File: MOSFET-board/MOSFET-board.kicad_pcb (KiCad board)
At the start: 2 copper layers, 88.9 x 76.2 mm, 116 parts, among them J1 PCIE-LP-01-01-F-DV-A-TR, J2 DB15_Female, J3 DB15_Female, U1 BTS3080EJXUMA1, U10 BTS3080EJXUMA1, U11 PCF8575_Breakout, U12 INA193, U13 INA193, U14 INA193, U15 INA193, U16 INA193, U17 INA193, U18 INA193, U19 INA193, U2 BTS3080EJXUMA1, U20 INA193, U21 INA193, U3 BTS3080EJXUMA1, U4 BTS3080EJXUMA1, U5 BTS3080EJXUMA1, U6 BTS3080EJXUMA1, U7 BTS3080EJXUMA1, U8 BTS3080EJXUMA1, U9 BTS3080EJXUMA1

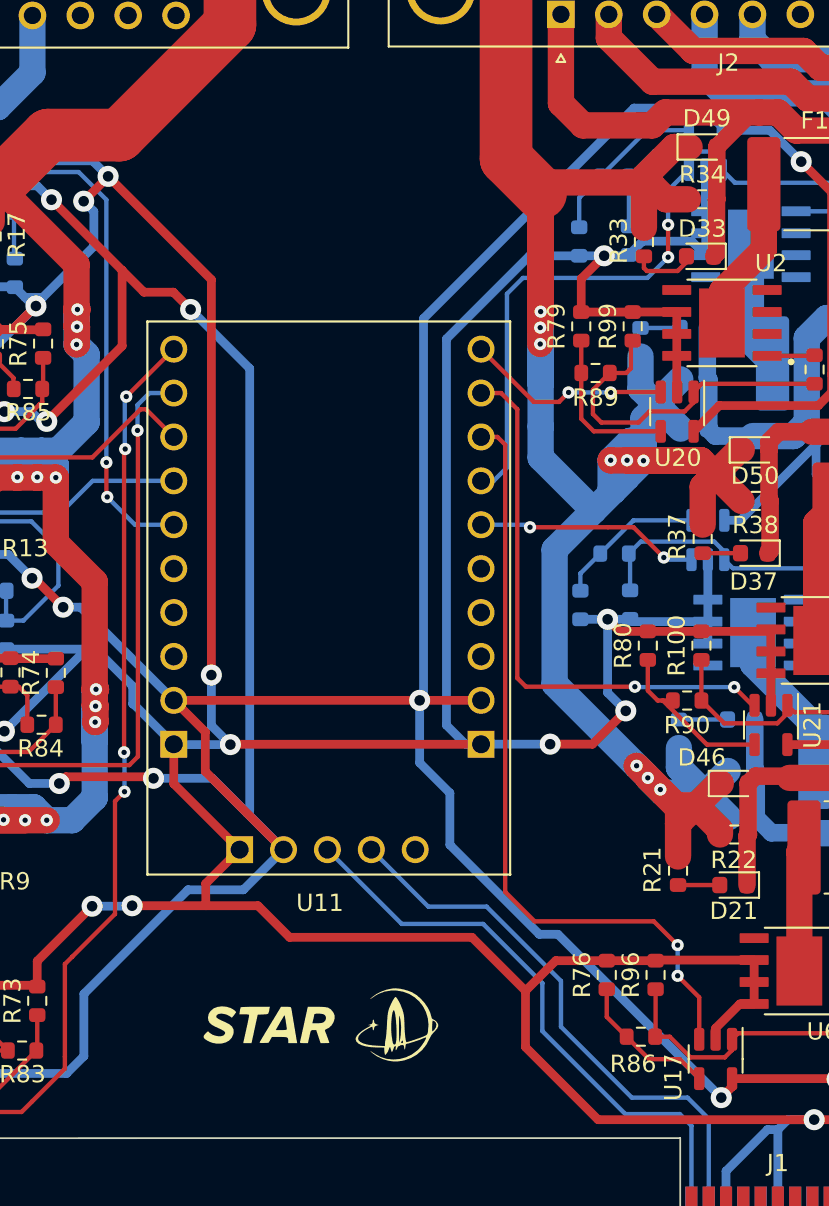
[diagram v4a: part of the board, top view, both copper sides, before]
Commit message: MOSFET Board Updated (Part II)
Added double header GPIO and should be fine now :P
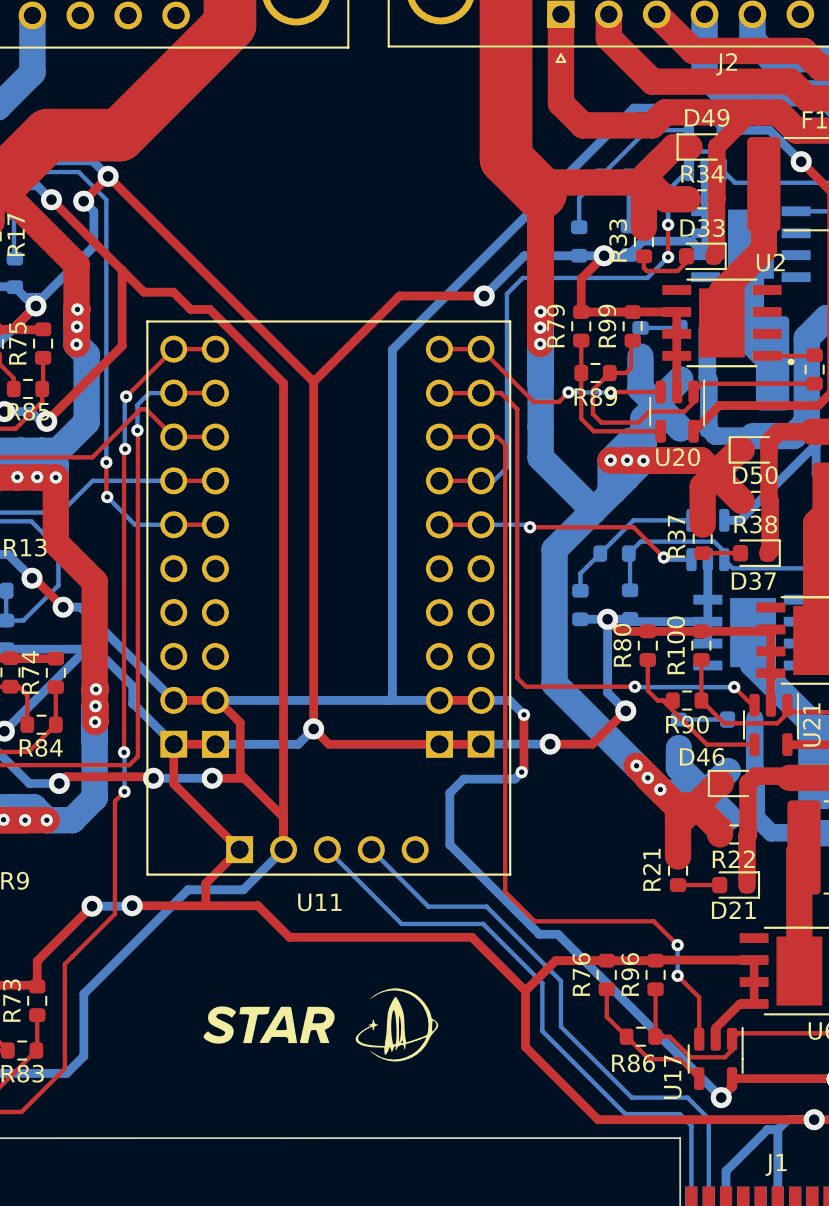
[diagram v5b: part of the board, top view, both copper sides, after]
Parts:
- added ?: , , F.Cu at (169.0, 104.2)
- added ?: , , F.Cu at (156.0, 94.0)
- added ?: , , F.Cu at (169.0, 116.9)
- added ?: , , F.Cu at (156.0, 114.4)
- added ?: , , F.Cu at (156.0, 104.2)
- added ?: , , F.Cu at (169.0, 101.7)
- added ?: , , F.Cu at (169.0, 99.1)
- added ?: , , F.Cu at (169.0, 111.8)
- added ?: , , F.Cu at (156.0, 106.8)
- added ?: , , F.Cu at (156.0, 101.7)
- added ?: , , F.Cu at (169.0, 114.4)
- added ?: , , F.Cu at (156.0, 116.9)
- added ?: , , F.Cu at (156.0, 96.6)
- added ?: , , F.Cu at (156.0, 111.8)
- added ?: , , F.Cu at (156.0, 99.1)
- added ?: , , F.Cu at (169.0, 94.0)
- added ?: , , F.Cu at (156.0, 109.3)
- added ?: , , F.Cu at (169.0, 106.8)
- added ?: , , F.Cu at (169.0, 109.3)
- added ?: , , F.Cu at (169.0, 96.6)
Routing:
- net GND: track 449.1 -> 434.8 mm
- net +5V: track 332.0 -> 336.7 mm, vias 16 -> 17
- net PYRO3EN: track 36.4 -> 38.8 mm
- net PYRO9EN: track 35.1 -> 37.6 mm
- net PYRO1EN: track 53.7 -> 56.1 mm
- net PYRO6EN: track 44.7 -> 47.1 mm
- net PYRO10EN: track 13.0 -> 15.4 mm
- net PYRO7EN: track 18.8 -> 21.2 mm
- net PYRO5EN: track 17.4 -> 19.8 mm
- net PYRO8EN: track 27.6 -> 30.0 mm
- net PYRO4EN: track 32.4 -> 34.8 mm
- net PYRO2EN: track 11.9 -> 14.3 mm

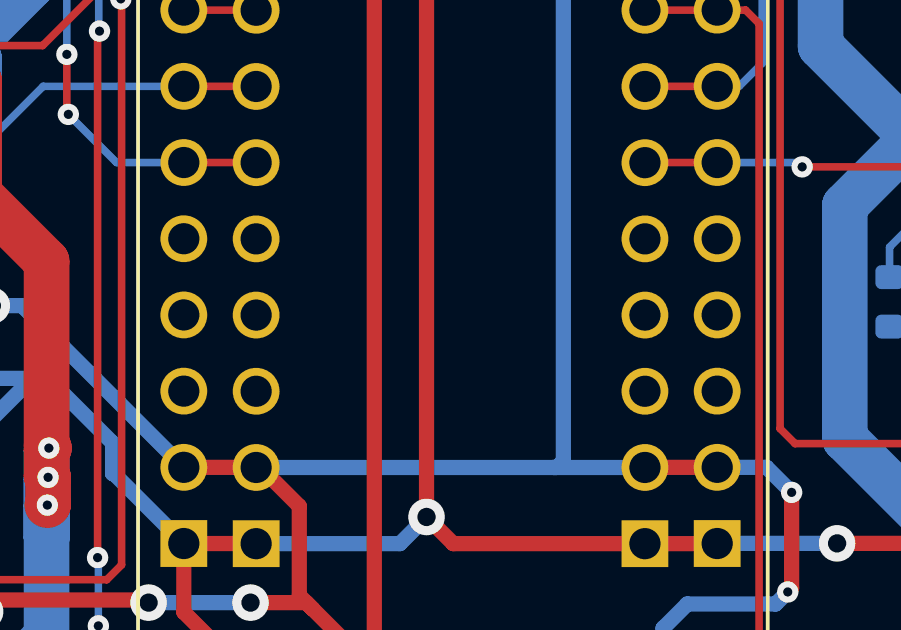
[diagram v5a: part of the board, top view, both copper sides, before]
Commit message: Updated MOSFET (part III)
Made sure there were 0 errors.
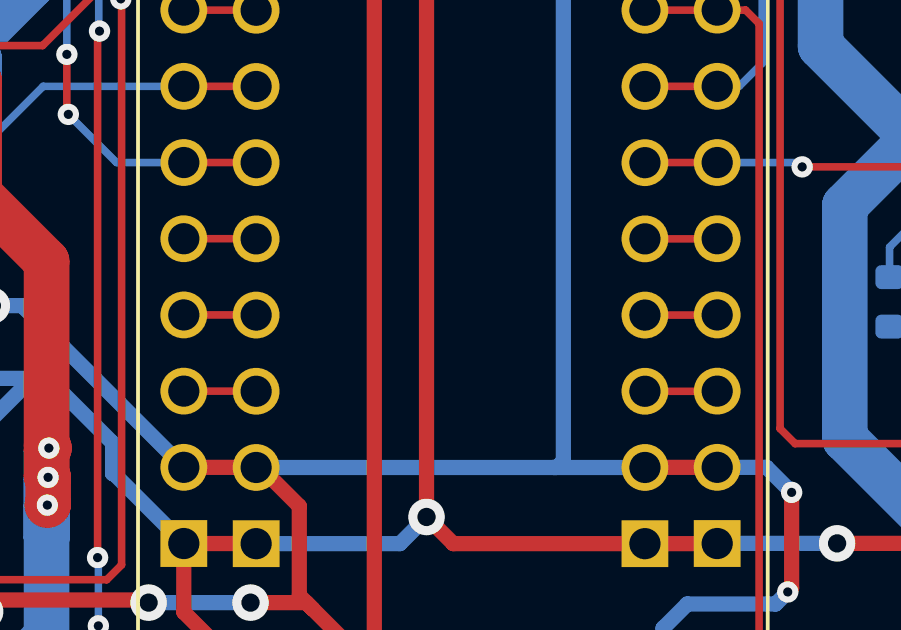
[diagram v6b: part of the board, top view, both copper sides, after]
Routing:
- net unconnected-(U11-P16-Pad7): track 0.00 -> 2.41 mm
- net unconnected-(U11-P17-Pad8): track 0.00 -> 2.41 mm
- net unconnected-(U11-P15-Pad6): track 0.00 -> 2.41 mm
- net unconnected-(U11-P01-Pad19): track 0.00 -> 2.41 mm
- net unconnected-(U11-P02-Pad20): track 0.00 -> 2.41 mm
- net unconnected-(U11-P00-Pad18): track 0.00 -> 2.41 mm
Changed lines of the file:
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@@
   (segment (start 195.45 112.9) (end 195.45 112.875) (width 0.254) (layer "F.Cu") (net 104))
   (segment (start 195.95 113.4) (end 195.45 112.9) (width 0.254) (layer "F.Cu") (net 104))
+  (segment (start 153.5989 106.7455) (end 156.0055 106.7455) (width 0.254) (layer "F.Cu") (net 145))
+  (segment (start 156.0055 106.7455) (end 156.01 106.75) (width 0.254) (layer "F.Cu") (net 145))
+  (segment (start 156.0055 109.2855) (end 156.01 109.29) (width 0.254) (layer "F.Cu") (net 146))
+  (segment (start 153.5989 109.2855) (end 156.0055 109.2855) (width 0.254) (layer "F.Cu") (net 146))
+  (segment (start 156.0055 111.8255) (end 156.01 111.83) (width 0.254) (layer "F.Cu") (net 147))
+  (segment (start 153.5989 111.8255) (end 156.0055 111.8255) (width 0.254) (layer "F.Cu") (net 147))
+  (segment (start 168.97 111.83) (end 171.37384 111.83) (width 0.254) (layer "F.Cu") (net 149))
+  (segment (start 171.37384 111.83) (end 171.37834 111.8255) (width 0.254) (layer "F.Cu") (net 149))
+  (segment (start 171.37384 109.29) (end 171.37834 109.2855) (width 0.254) (layer "F.Cu") (net 150))
+  (segment (start 168.97 109.29) (end 171.37384 109.29) (width 0.254) (layer "F.Cu") (net 150))
+  (segment (start 171.37384 106.75) (end 171.37834 106.7455) (width 0.254) (layer "F.Cu") (net 151))
+  (segment (start 168.97 106.75) (end 171.37384 106.75) (width 0.254) (layer "F.Cu") (net 151))
   (zone (net 25) (net_name "GND") (layers "F&B.Cu") (hatch edge 0.508)
     (connect_pads (clearance 0.508))

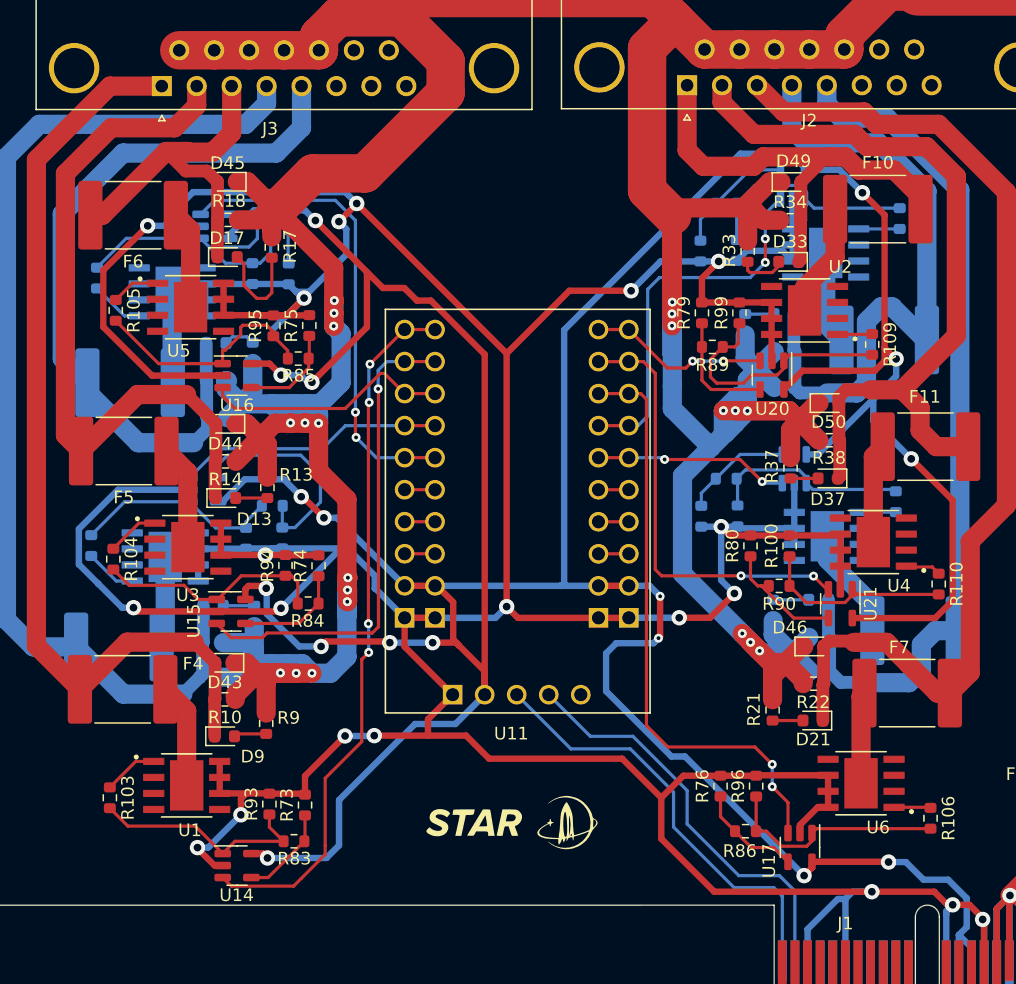
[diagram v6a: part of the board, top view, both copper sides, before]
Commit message: MOSFET Board Updated (Part IV? I lost count)
Has a specified op amp, fixed measurements, should be a double header GPIO, I believe that everything is connected. The only warnings are either silk screen or non labeled items, which should be fine.
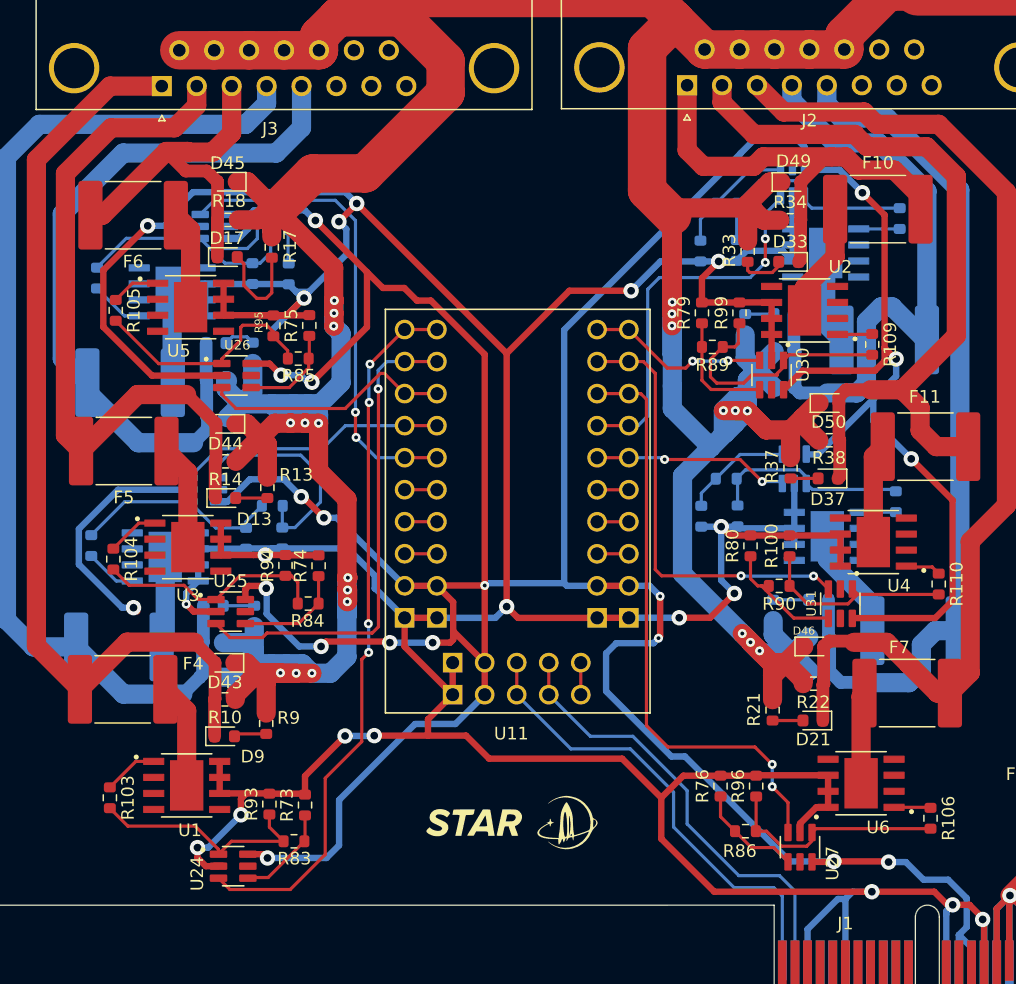
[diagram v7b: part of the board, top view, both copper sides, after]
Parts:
- removed U12, U13, U14, U15, U16, U17, U18, U19, U20, U21: INA193, Package_TO_SOT_SMD:SOT-23-5
- added ?: , , F.Cu at (159.9, 120.5)
- added ?: , , F.Cu at (157.4, 120.5)
- added ?: , , F.Cu at (162.5, 120.5)
- added ?: , , F.Cu at (165.0, 120.5)
- added ?: , , F.Cu at (167.6, 120.5)
- added U22: ADA4897-1ARJZ-R7, Symbol:SOT95P280X145-6N, B.Cu at (137.7, 106.8)
- added U23: ADA4897-1ARJZ-R7, Symbol:SOT95P280X145-6N, B.Cu at (138.6, 85.9)
- added U24: ADA4897-1ARJZ-R7, Symbol:SOT95P280X145-6N, F.Cu at (140.0, 136.6)
- added U25: ADA4897-1ARJZ-R7, Symbol:SOT95P280X145-6N, F.Cu at (139.8, 116.4)
- added U26: ADA4897-1ARJZ-R7, Symbol:SOT95P280X145-6N, F.Cu at (140.3, 97.7)
- added U27: ADA4897-1ARJZ-R7, Symbol:SOT95P280X145-6N, F.Cu at (184.9, 135.1)
- added U28: ADA4897-1ARJZ-R7, Symbol:SOT95P280X145-6N, B.Cu at (184.4, 82.3)
- added U29: ADA4897-1ARJZ-R7, Symbol:SOT95P280X145-6N, B.Cu at (184.5, 105.1)
- added U30: ADA4897-1ARJZ-R7, Symbol:SOT95P280X145-6N, F.Cu at (182.7, 97.7)
- added U31: ADA4897-1ARJZ-R7, Symbol:SOT95P280X145-6N, F.Cu at (188.2, 115.8)
- moved ? 0.15 mm to (156.2, 94.0)
- moved ? 0.15 mm to (156.2, 114.4)
- moved ? 0.15 mm to (156.2, 104.2)
- moved ? 0.15 mm to (156.2, 116.9)
- moved ? 0.15 mm to (156.2, 106.8)
- moved ? 0.15 mm to (156.2, 101.7)
- moved ? 0.15 mm to (156.2, 96.6)
- moved ? 0.15 mm to (156.2, 111.8)
- moved ? 0.15 mm to (156.2, 99.1)
- moved ? 0.15 mm to (156.2, 109.3)
- moved ? 0.11 mm to (168.9, 104.2)
- moved ? 0.11 mm to (168.9, 96.6)
- moved ? 0.11 mm to (168.9, 116.9)
- moved ? 0.11 mm to (168.9, 101.7)
- moved ? 0.11 mm to (168.9, 99.1)
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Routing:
- net GND: track 434.8 -> 422.9 mm
- net I2C_SDA: track 34.4 -> 37.0 mm
- net I2C_SCL: track 33.6 -> 36.1 mm
- net unconnected-(U11-INT-Pad15): track 0.00 -> 2.54 mm
- net +12V: track 457.7 -> 455.7 mm
- net PYRO8: track 51.4 -> 50.1 mm
- net Net-(R107-Pad2): track 17.4 -> 18.2 mm
- net PYRO1EN: track 56.1 -> 56.8 mm
- net Net-(R72-Pad1): track 13.7 -> 14.3 mm
- net Net-(R106-Pad2): track 18.0 -> 17.4 mm
- net +5V: track 336.7 -> 337.1 mm, vias 17 -> 18
